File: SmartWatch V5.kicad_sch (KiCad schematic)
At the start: 59 parts, among them J1 10118192-0001LF, J10 TestPad, J8 TestPad, J9 TestPad, Q1 FDN340P, Q2 MMBT3904, Q3 MMBT3904, Q5 FDN028N20, Q6 FDN028N20, SW1 EVQ-P7J01P, SW2 EVQ-P7J01P, U1 MAX17260, U10 TSC2003IPWR, U2 FT231XQ, U3 LP5912-3.3DRVT, U5 MCP73832-2-OT, U6 ESP32-WROOM-32, U8 ADXL337

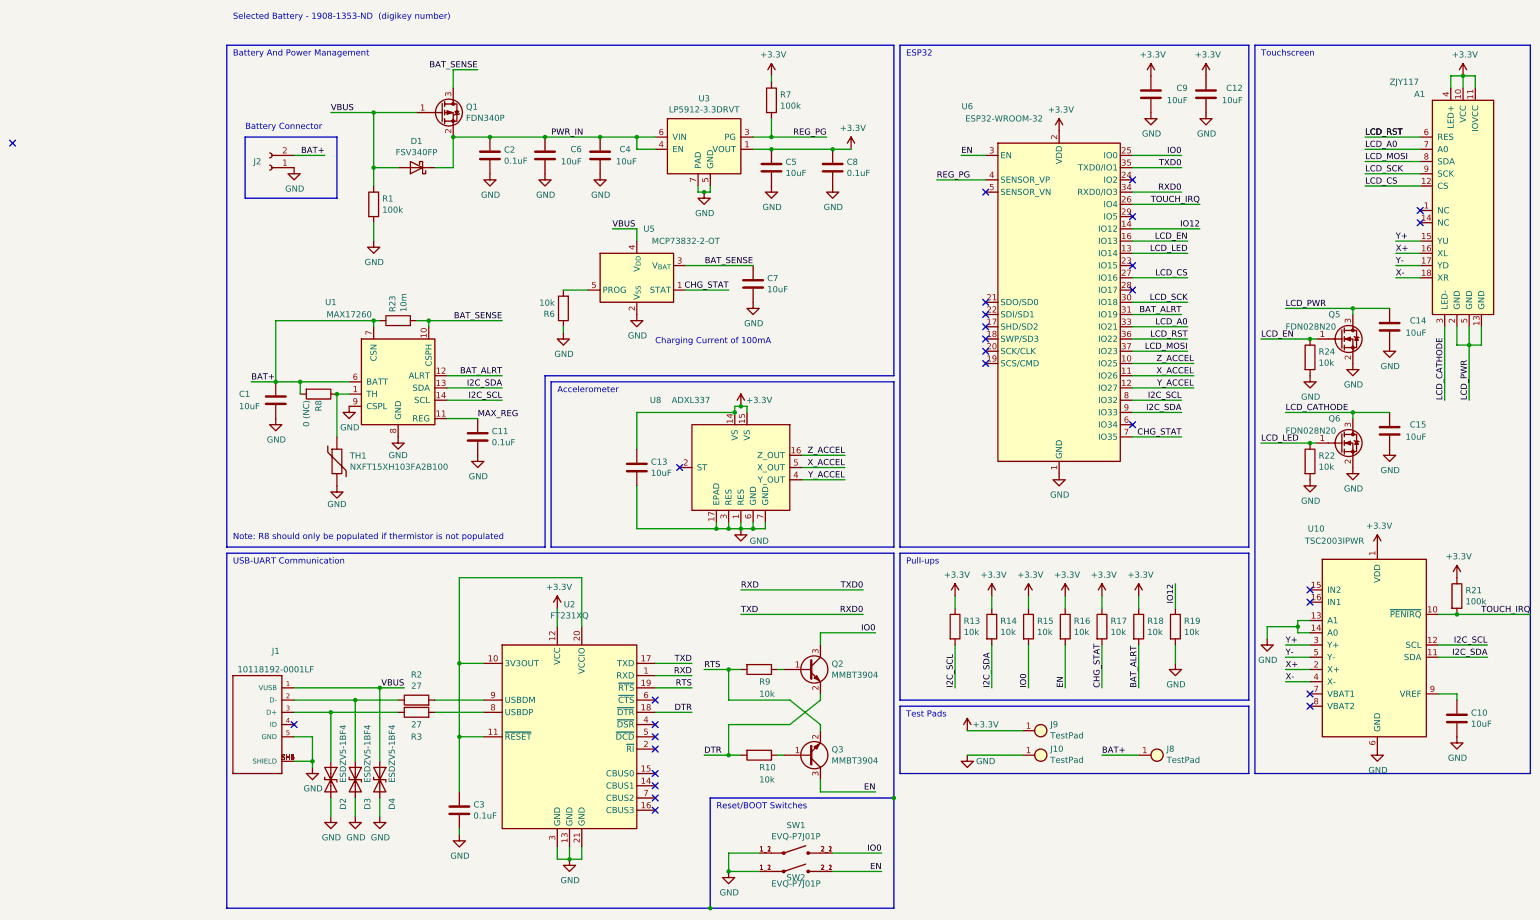
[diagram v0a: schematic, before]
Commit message: Updated part parameters
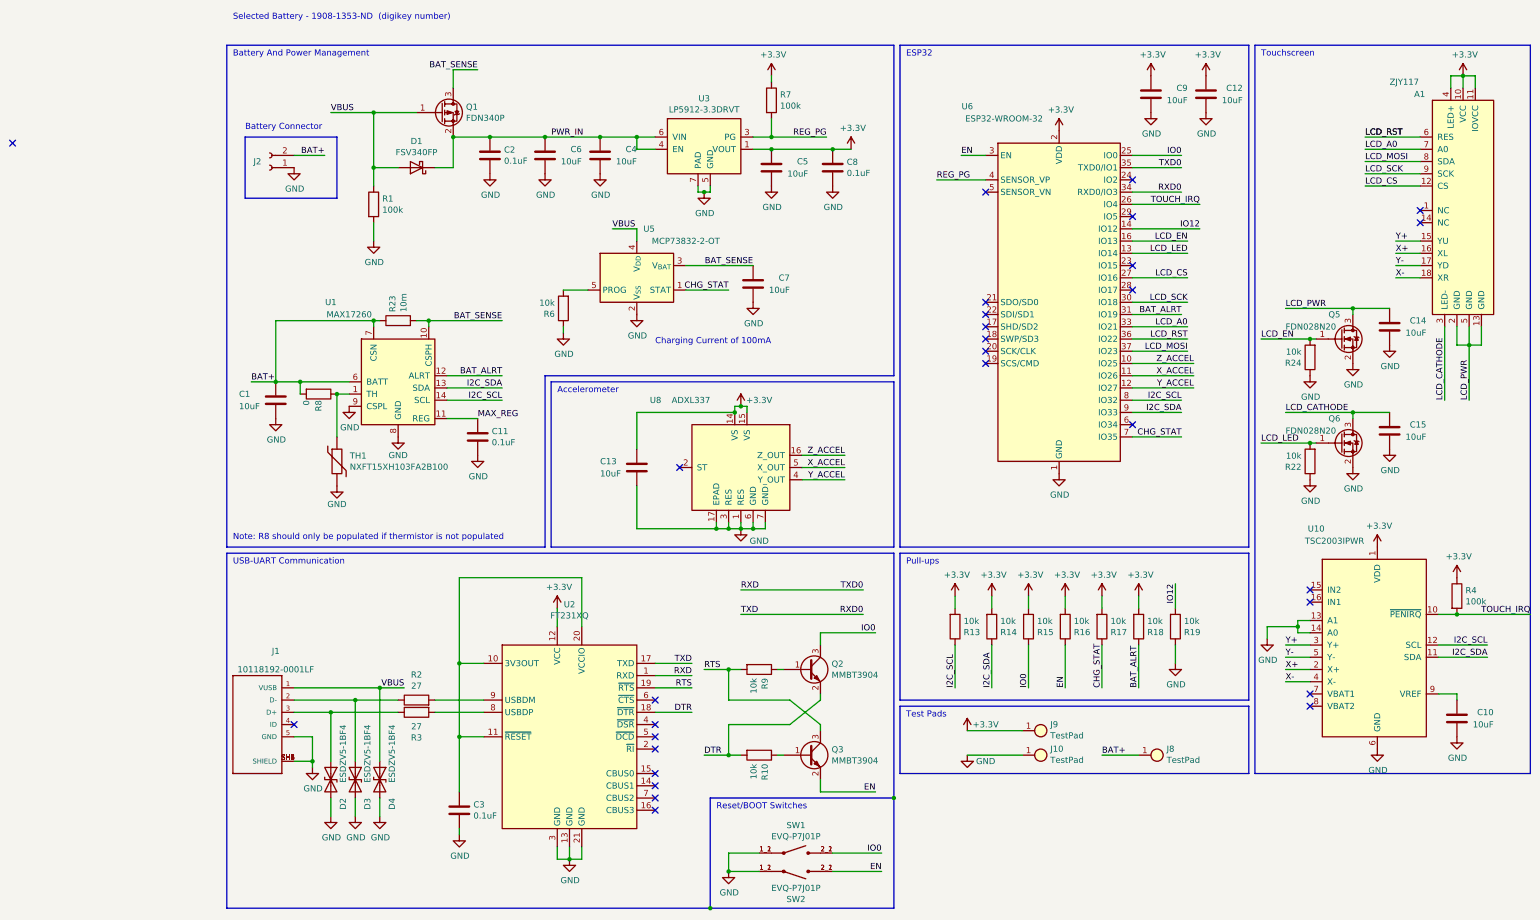
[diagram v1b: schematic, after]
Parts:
- removed R21: 100k, Resistor_SMD:R_0603_1608Metric, symbol Device:R
- added R4: 100k, Resistor_SMD:R_0603_1608Metric, symbol Device:R
- A1: Area (none) -> 28 mm × 22 mm; Backlight (none) -> LED; Protocol (none) -> SPI; Resolution (none) -> 160 × 128; Touchscreen (none) -> Resistive; Voltage (none) -> 3.3V
- C1, C10, C12, C13, C14, C15, C4, C5, C6, C7, C9: Digikey (none) -> 478-10766-1-ND; MPN (none) -> 0603ZD106KAT2A; Operating Temperature (none) -> -55°C ~ 85°C; Temp Co (none) -> X5R; Voltage (none) -> 10V; digikey 478-10766-1-ND -> (none)
- C11, C2, C3, C8: Digikey (none) -> 1276-1006-1-ND; MPN (none) -> CL10B104KA8NNNC; Operating Temperature (none) -> -55°C ~ 125°C; Temp Co (none) -> X7R; Tolerance (none) -> 10%; Voltage (none) -> 25V; digikey 1276-1006-1-ND -> (none)
- D1: Current (none) -> 3A; Digikey (none) -> FSV340FPCT-ND; Operating Temperature (none) -> -55°C ~ 150°C; Voltage (none) -> 40V; digikey FSV340FPCT-ND -> (none)
- D2, D3, D4: Clamping Voltage (none) -> 10V; Current (none) -> 7A; Digikey (none) -> 497-17318-1-ND; Operating Temperature (none) -> -55°C ~ 150°C (TJ); Power (none) -> 70W; Type (none) -> Zener; Zener Voltage (none) -> 5.5V; digikey 497-17318-1-ND -> (none)
- J1: Digikey (none) -> 609-4613-1-ND; Field4 None -> (none); Field5 Single Port 5 Contact Horizontal Right Angle Shielded Micro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 -> (none); Field7 10118192-0001LF -> (none); Field8 https://www.digikey.com/product-detail/en/amphenol-icc-fci/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 -> (none); Gender (none) -> Female; MPN (none) -> 10118192-0001LF; Mounting (none) -> Surface Mount, Right Angle; Type (none) -> USB - micro B; digikey 609-4613-1-ND -> (none)
- J2: value (none) -> ~
- Q1: Current (none) -> 2A; Digikey (none) -> FDN340PCT-ND; Operating Temperature (none) -> -55°C ~ 150°C (TJ); Type (none) -> P-Channel; Voltage (none) -> 20V; digikey FDN340PCT-ND -> (none)
- Q2, Q3: Current (none) -> 200mA; Digikey (none) -> 1727-4044-1-ND; Power (none) -> 250mW; Type (none) -> NPN; Voltage (none) -> 40V; digikey 1727-4044-1-ND -> (none)
- Q5, Q6: Current (none) -> 6.1A; Digikey (none) -> FDN028N20OSCT-ND; Power (none) -> 1.5W; Type (none) -> N-Channel; Voltage (none) -> 20V; digikey FDN028N20OSCT-ND -> (none)
- R1, R7: Digikey (none) -> CR0603-JW-104ELFCT-ND; Power Rating (none) -> 0.1W; Tolerance (none) -> 5%; digikey CR0603-JW-104ELFCT-ND -> (none)
- R10, R13, R14, R15, R16, R17, R18, R19, R22, R24, R6, R9: Digikey (none) -> 311-10.0KCRCT-ND; MPN (none) -> RC0805FR-0710KL; Operating Temperature (none) -> -55°C ~ 155°C; Power (none) -> 0.125W; Tolerance (none) -> 1%; digikey 311-10.0KCRCT-ND -> (none)
- R2, R3: Digikey (none) -> RMCF0603JT27R0CT-ND; MPN (none) -> RMCF0603JT27R0; Operating Temperature (none) -> -55°C ~ 155°C; Power (none) -> 0.1W; Tolerance (none) -> 5%; digikey RMCF0603JT27R0CT-ND -> (none)
- R23: Digikey (none) -> RL12T.010JCT-ND; Operating Temperature (none) -> -55°C ~ 125°C; Power Rating (none) -> 0.25W; Tolerance (none) -> 5%; digikey RL12T.010JCT-ND -> (none)
- R8: value 0 (NC) -> 0; Digikey (none) -> 311-0.0GRCT-ND; MPN (none) -> RC0603JR-070RL; Temperature Rating (none) -> -55°C ~ 155°C; digikey 311-0.0GRCT-ND -> (none)
- SW1, SW2: Circuit (none) -> SPST-NO; Digikey (none) -> P16767CT-ND; Field4 Manufacturer Recommendation -> (none); Mounting (none) -> Surface Mount, Right Angle; digikey P16767CT-ND -> (none)
- TH1: B25/85 (none) -> 3434K; Digikey (none) -> 490-5630-ND; Nominal Resistance (none) -> 10k; Operating Temperature (none) -> -40°C ~ 125°C; Power (none) -> 100mW; Tolerance (none) -> 1%; digikey 490-5630-ND -> (none)
- U1: Battery Chemistry (none) -> Li-ion; Cell Count (none) -> 1; Digikey (none) -> 175-MAX17260SEWL+TCT-ND; Interface (none) -> I2C; Operating Temperature (none) -> -40°C ~ 85°C; digikey 175-MAX17260SEWL+TCT-ND -> (none)
- U10: Digikey (none) -> 296-14340-1-ND; Interface (none) -> I2C; Operating Temperature (none) -> -40°C ~ 85°C; Resolution (none) -> 12b; Type (none) -> Resistive; digikey 296-14340-1-ND -> (none)
- U2: Digikey (none) -> 768-1128-1-ND; Operating Temperature (none) -> -40°C ~ 85°C; Protocol (none) -> USB; Voltage Range (none) -> 3.3V ~ 5V; digikey 768-1128-1-ND -> (none)
- U3: Digikey PN (none) -> 296-44153-1-ND; Operating Temperature (none) -> -40°C ~ 125°C (TJ); Voltage (none) -> 6.5V; digikey 296-44153-1-ND -> (none)
- U5: Cells (none) -> 1; Charge Current (none) -> 500mA; Digikey (none) -> MCP73832T-2ACI/OTCT-ND; Operating Temperature (none) -> -40°C ~ 85°C (TA); Voltage (none) -> 6V; digikey MCP73832T-2ACI/OTCT-ND -> (none)
- U6: Communications (none) -> Bluetooth, WiFi; Digikey (none) -> 1904-1010-1-ND; MPN (none) -> ESP32-WROOM-32-N4; Operating Temperature (none) -> -40°C ~ 85°C; Voltage Max (none) -> 3.6V; Voltage Min (none) -> 2.7V; digikey 1904-1010-1-ND -> (none)
- U8: Axis (none) -> X, Y, Z; Digikey (none) -> ADXL337BCPZ-RLCT-ND; Operating Tmperature (none) -> -40°C ~ 85°C; Range (none) -> 3g; Type (none) -> Analog; digikey ADXL337BCPZ-RLCT-ND -> (none)
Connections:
- net +3.3V: now also R13.2, R14.2, R15.2, R16.2, R17.2, R18.2, R4.1; no longer R13.1, R14.1, R15.1, R16.1, R17.1, R18.1
- net BAT_ALRT: now also R18.1; no longer R18.2
- net CHG_STAT: now also R17.1; no longer R17.2
- net EN: now also Q3.2 (E), R16.1; no longer Q3.3 (C), R16.2
- net GND: now also R19.1, R22.1, R24.1; no longer R19.2, R22.2, R24.2
- net I2C_SCL: now also R13.1; no longer R13.2
- net I2C_SDA: now also R14.1; no longer R14.2
- net IO0: now also R15.1; no longer R15.2
- net IO12: now also R19.2; no longer R19.1
- net LCD_EN: now also R24.2; no longer R24.1
- net LCD_LED: now also R22.2; no longer R22.1
- net RTS: now also Q3.3 (C); no longer Q3.2 (E)
- net TOUCH_IRQ: now also R4.2
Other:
- company: (none) -> xAI

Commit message: Updated accel to newer model
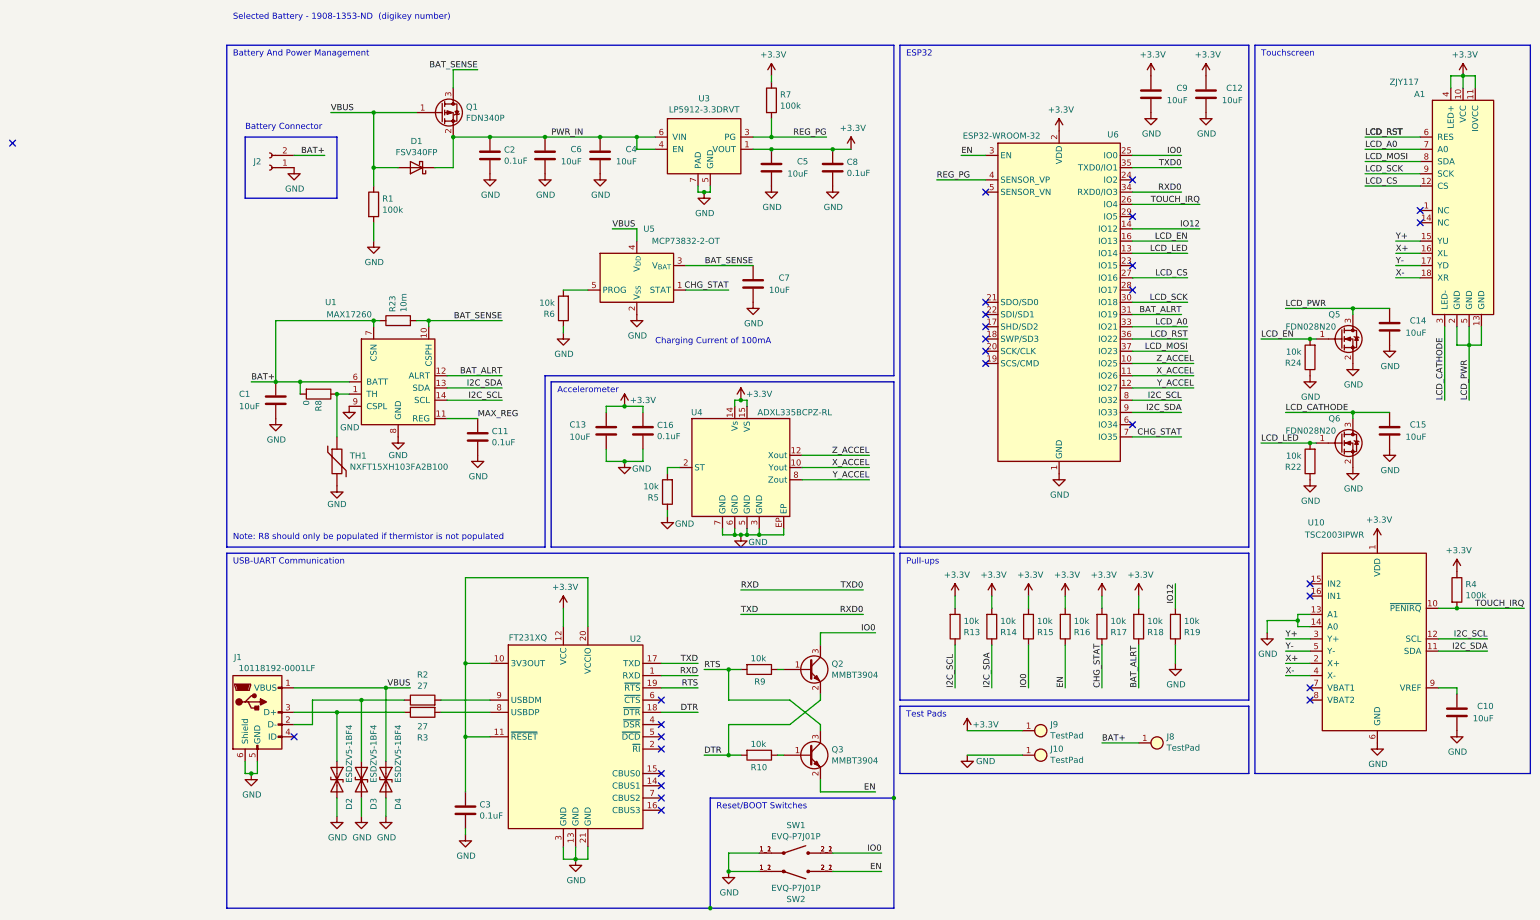
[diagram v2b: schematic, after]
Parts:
- removed U8: ADXL337, CustomFootprints:ADXL337BCPZ-RL, symbol CustomParts:ADXL337
- added C16: 0.1uF, Capacitor_SMD:C_0603_1608Metric, symbol Device:C
- added R5: 10k, Resistor_SMD:R_0603_1608Metric, symbol Device:R
- added U4: ADXL335BCPZ-RL, Package_CSP:Analog_LFCSP-16-1EP_4x4mm_P0.65mm_EP2.35x2.35mm, symbol symbol_library:ADXL335BCPZ-RL
- J1: symbol CustomParts:10118192-0001LF -> Connector:USB_B_Micro
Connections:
- net +3.3V: now also C16.1, U4.14 (Vs), U4.15 (VS)
- net GND: now also J1.6 (Shield), C16.2, R5.1, U4.3 (GND), U4.5 (GND), U4.6 (GND), U4.7 (GND), U4.EP; no longer J1.SH1 (SHIELD), J1.SH2 (SHIELD), J1.SH3 (SHIELD), J1.SH4 (SHIELD), J1.SH5 (SHIELD), J1.SH6 (SHIELD)
- net X_ACCEL: now also U4.10 (Yout)
- net Y_ACCEL: now also U4.8 (Zout)
- net Z_ACCEL: now also U4.12 (Xout)
- new net: R5.2, U4.2 (ST)
- new net: U4.1 (NC), U4.11 (NC), U4.13 (NC), U4.16 (NC), U4.4 (NC), U4.9 (NC)
- no-connect marks 29 -> 28
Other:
- moved on the sheet: C10, C13, C3, D2, D3, D4, J8, R2, R3, R4, U10, U2

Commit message: revert kicad_sch for testing
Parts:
- removed C16: 0.1uF, Capacitor_SMD:C_0603_1608Metric, symbol Device:C
- removed R5: 10k, Resistor_SMD:R_0603_1608Metric, symbol Device:R
- removed U4: ADXL335BCPZ-RL, Package_CSP:Analog_LFCSP-16-1EP_4x4mm_P0.65mm_EP2.35x2.35mm, symbol symbol_library:ADXL335BCPZ-RL
- added U8: ADXL337, CustomFootprints:ADXL337BCPZ-RL, symbol CustomParts:ADXL337
- J1: symbol Connector:USB_B_Micro -> CustomParts:10118192-0001LF
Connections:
- net +3.3V: now also U8.14 (VS), U8.15 (VS)
- net GND: now also J1.SH1 (SHIELD), J1.SH2 (SHIELD), J1.SH3 (SHIELD), J1.SH4 (SHIELD), J1.SH5 (SHIELD), J1.SH6 (SHIELD), U8.1 (RES), U8.17 (EPAD), U8.3 (RES), U8.6 (GND), U8.7 (GND); no longer J1.6 (Shield)
- net X_ACCEL: now also U8.5 (X_OUT)
- net Y_ACCEL: now also U8.4 (Y_OUT)
- net Z_ACCEL: now also U8.16 (Z_OUT)
- no-connect marks 28 -> 29
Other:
- moved on the sheet: C10, C13, C3, D2, D3, D4, J8, R2, R3, R4, U10, U2
